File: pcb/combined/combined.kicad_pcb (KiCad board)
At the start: 2 copper layers, 65 x 38 mm, 34 parts, among them J1 CTRL, J2 MAINS_IN, J3 VALVE, J4 PUMP, Q1 SS8050, Q2 BT136S, Q3 SS8050, Q4 BT136S, U1 MOC3043M, U2 MOC3023M, U3 EL817C

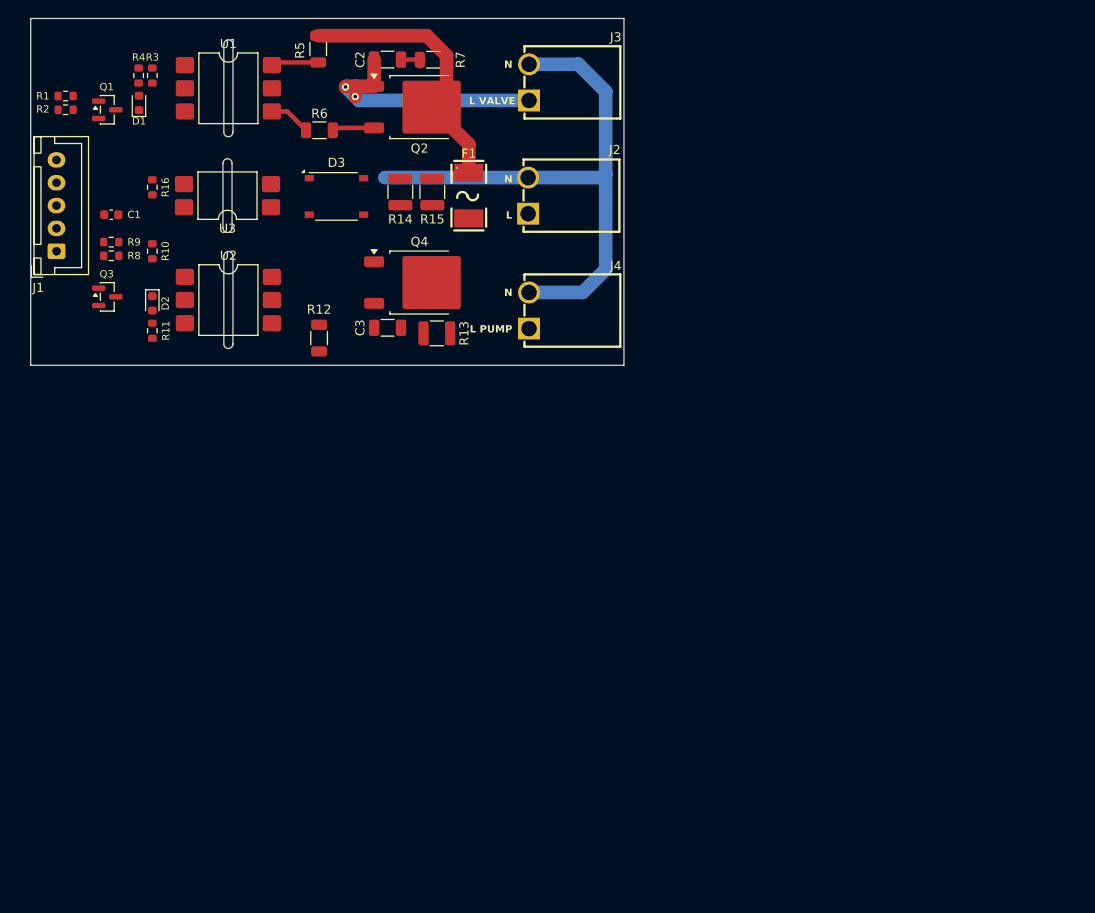
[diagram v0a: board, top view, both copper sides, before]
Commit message: Combine the AC control and sensors circuits on the combined board
The renamed accontrol project now carries the sensors controller on two
new sheets: XIAO, CAN, I2C pull-ups with TMP102 and ADS1115, FLOW, boiler
output, status LED and the 5 V, CAN, BOILER, PRESSURE and FLOW headers.
The 5-pin control header, the Grove I2C headers and the VALVE header are
dropped: DIM, ZC and SSR run as tracks to XIAO D0, D2 and D10. Sensors
parts that clashed with AC references are renumbered, the BOM and design
notes follow, and +5V/+3V3 get the 0.3 mm POWER net class from sensors.

Co-Authored-By: Claude Opus 5.5 <noreply@anthropic.com>
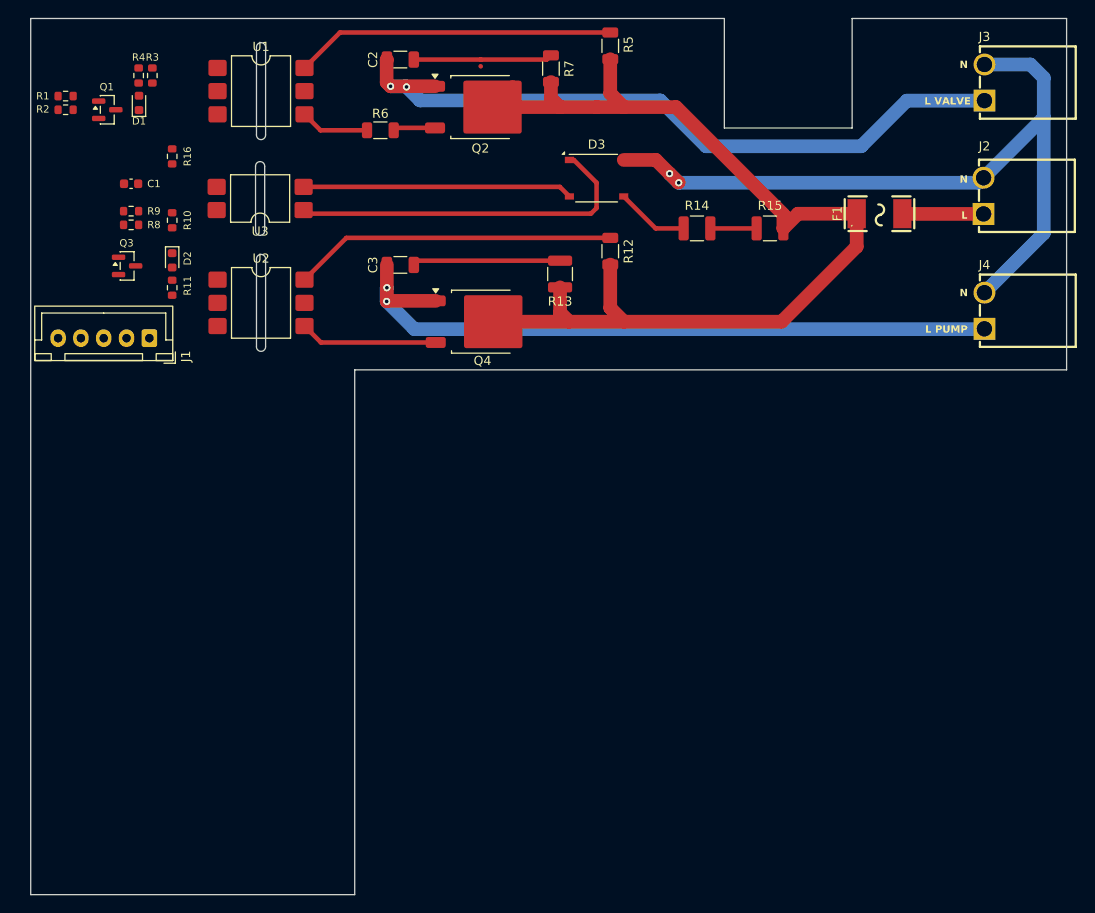
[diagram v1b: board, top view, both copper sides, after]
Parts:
- F1: footprint Accontrol_Local:F2410 -> Combined_Local:F2410
- J2, J3, J4: footprint Accontrol_Local:CONN-TH_P3.96_HT396R-3.96-2P -> Combined_Local:CONN-TH_P3.96_HT396R-3.96-2P
- U1, U2: footprint Accontrol_Local:SMDIP-6_W9.53mm_Slot -> Combined_Local:SMDIP-6_W9.53mm_Slot
- U3: footprint Accontrol_Local:SMDIP-4_W9.53mm_Slot -> Combined_Local:SMDIP-4_W9.53mm_Slot
- moved J2 49.9 mm to (184.9, 66.4)
- moved J3 49.9 mm to (185.0, 54.0)
- moved J4 49.9 mm to (185.0, 79.0)
- moved F1 45.0 mm to (173.5, 68.4), turned to 0 degrees
- moved R15 37.2 mm to (161.5, 70.0), turned to 0 degrees
- moved R12 33.3 mm to (144.0, 72.5)
- moved R14 32.7 mm to (153.5, 70.0), turned to 0 degrees
- moved R5 32.0 mm to (144.0, 50.0), turned to -90 degrees
- moved D3 28.6 mm to (142.5, 64.5)
- moved R13 15.0 mm to (138.5, 75.0), turned to 90 degrees
- moved J1 13.9 mm to (93.5, 82.0), turned to 180 degrees
- moved R7 12.9 mm to (137.5, 52.5), turned to 90 degrees
- moved Q4 8.00 mm to (129.9, 80.2)
- moved C3 7.03 mm to (121.0, 74.0)
- moved Q2 6.67 mm to (129.8, 56.7)
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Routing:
- net /L: track 30.2 -> 117.0 mm
- net /L_PUMP: track 0.00 -> 77.6 mm, vias 0 -> 2
- net /L_VALVE: track 27.9 -> 77.9 mm
- net Net-(D3-+): track 0.00 -> 40.0 mm
- net Net-(R12-Pad1): track 0.00 -> 35.4 mm
- net Net-(R5-Pad1): track 5.38 -> 35.3 mm
- net Net-(D3--): track 0.00 -> 29.6 mm
- net /N: track 63.0 -> 84.8 mm, vias 0 -> 2
- net Net-(C3-Pad1): track 0.00 -> 16.2 mm
- net Net-(Q4-G): track 0.00 -> 15.1 mm
- net Net-(C2-Pad1): track 2.10 -> 15.3 mm
- net /L_IN: track 0.00 -> 8.91 mm
- net Net-(D3-Pad3): track 0.00 -> 8.01 mm
- net Net-(R14-Pad2): track 0.00 -> 5.07 mm
- net Net-(R6-Pad1): track 4.60 -> 7.57 mm
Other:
- board size 65 x 38 mm -> 113.5 x 96 mm

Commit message: Bring the sensors footprints onto the combined board and align the XIAO sockets
Update the combined PCB from the schematic, which adds the sensors
footprints and replaces the old 5-pin control header. A board-only XIAO
outline footprint, without pads or drills, marks the module and its 14 pin
centres; J11 (turned 180 degrees, DIM at the bottom) and J12 sit exactly
on those centres.

Co-Authored-By: Claude Opus 5.5 <noreply@anthropic.com>
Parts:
- added C10: 100nF, Capacitor_SMD:C_0603_1608Metric, F.Cu at (87.0, 63.0)
- added C12: 10nF, Capacitor_SMD:C_0603_1608Metric, F.Cu at (84.3, 80.0)
- added C13: 100nF, Capacitor_SMD:C_0603_1608Metric, F.Cu at (105.2, 111.5)
- added C14: 10uF, Capacitor_SMD:C_0603_1608Metric, F.Cu at (114.0, 111.5)
- added C15: 100nF, Capacitor_SMD:C_0603_1608Metric, F.Cu at (93.5, 123.5)
- added C8: 100nF, Capacitor_SMD:C_0603_1608Metric, F.Cu at (83.5, 114.5)
- added C9: 100nF, Capacitor_SMD:C_0603_1608Metric, F.Cu at (88.0, 114.5)
- added D4: GREEN / STATUS, LED_SMD:LED_0805_2012Metric, F.Cu at (104.5, 134.5)
- added H1: M2.5, MountingHole:MountingHole_2.7mm_M2.5, F.Cu at (93.5, 140.0)
- added J10: PRESSURE, Connector_JST:JST_XH_B3B-XH-A_1x03_P2.50mm_Vertical, F.Cu at (95.5, 128.4)
- added J11: XIAO D0-D6, Combined_Local:XIAO_Socket_1x07_P2.54mm_Vertical, F.Cu at (99.2, 103.2)
- added J12: XIAO D7-5V, Combined_Local:XIAO_Socket_1x07_P2.54mm_Vertical, F.Cu at (84.0, 88.0)
- added J5: CAN BUS, Connector_JST:JST_XH_B2B-XH-A_1x02_P2.50mm_Vertical, F.Cu at (83.5, 139.0)
- added J6: FLOW HALL, Connector_JST:JST_XH_B3B-XH-A_1x03_P2.50mm_Vertical, F.Cu at (83.5, 128.4)
- added J8: BOILER SSR, Connector_JST:JST_XH_B2B-XH-A_1x02_P2.50mm_Vertical, F.Cu at (98.0, 120.0)
- added Q5: AO3401A, Package_TO_SOT_SMD:SOT-23, F.Cu at (105.6, 106.0)
- added Q6: 2N7002, Package_TO_SOT_SMD:SOT-23, F.Cu at (103.1, 101.0)
- added R17: 10k, Resistor_SMD:R_0603_1608Metric, F.Cu at (93.0, 114.5)
- added R18: 120 / 0.25W, Resistor_SMD:R_1206_3216Metric, F.Cu at (82.0, 120.5)
- added R19: 100k, Resistor_SMD:R_0603_1608Metric, F.Cu at (99.5, 110.5)
- added R20: 4.7k, Resistor_SMD:R_0603_1608Metric, F.Cu at (96.3, 83.0)
- added R21: 10k, Resistor_SMD:R_0603_1608Metric, F.Cu at (106.7, 101.5)
- added R22: 1k, Resistor_SMD:R_0603_1608Metric, F.Cu at (98.5, 114.0)
- added R23: 4.7k, Resistor_SMD:R_0603_1608Metric, F.Cu at (93.3, 83.0)
- added R24: 1k, Resistor_SMD:R_0603_1608Metric, F.Cu at (84.2, 84.0)
- added R25: 1k, Resistor_SMD:R_0603_1608Metric, F.Cu at (99.0, 135.0)
- added R26: 1k, Resistor_SMD:R_0603_1608Metric, F.Cu at (111.0, 111.5)
- added U4: TJA1051T/3, Package_SO:SOIC-8_3.9x4.9mm_P1.27mm, F.Cu at (87.0, 120.6)
- added U5: TMP102AIDRLR, Package_TO_SOT_SMD:SOT-563, F.Cu at (83.7, 65.5)
- added U6: ADS1115IDGSR, Package_SO:TSSOP-10_3x3mm_P0.5mm, F.Cu at (107.0, 95.0)
- added XIAO: XIAO-ESP32-S3-Outline, Combined_Local:XIAO-ESP32-S3-Outline, F.Cu at (91.6, 95.6)
- J1: value CTRL -> 5V POWER; footprint Connector_JST:JST_XH_B5B-XH-A_1x05_P2.50mm_Vertical -> Connector_JST:JST_XH_B2B-XH-A_1x02_P2.50mm_Vertical
- moved J1 57.4 mm to (100.5, 139.0), turned to 0 degrees
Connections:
- J1 pad 2: +3V3 -> +5V
- R1 pad 1: /SSR -> SSR
- R16 pad 2: /ZC -> ZC
- R2 pad 1: /SSR -> SSR
- R8 pad 1: /DIM -> DIM
- R9 pad 1: /DIM -> DIM
- U3 pad 4: /ZC -> ZC
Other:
- outline, holes or cut-outs redrawn

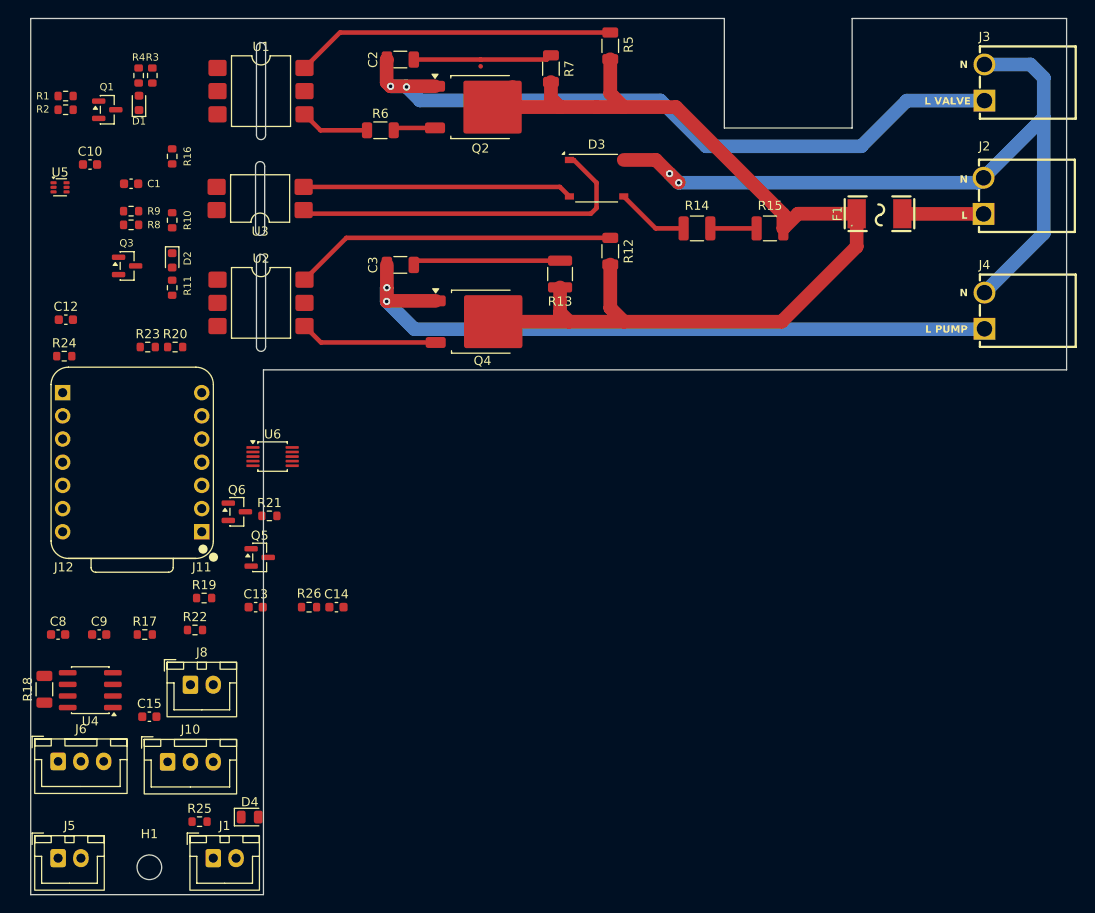
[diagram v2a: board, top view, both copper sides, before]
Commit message: Route the combined board to a clean DRC and export it for JLCPCB
Rules follow IEC 60335-1 for functional insulation: 2.2 mm between mains
nets, 1.5 mm or 1.1 mm between mains nets a few volts apart, and the
track-into-pad exception tied to the part a track enters. The HT3.96
connectors get oval pads, the datasheet's 1.6 mm holes and a milled slot
between L and N. C2/C3 move to 1812, R12 splits into R12 + R27, and every
part has its JLCPCB number. The exporter accepts polygon outlines, and the
placement corrections come from the supplier footprints. H2 and H3 are
added to the schematic.

Co-Authored-By: Claude Opus 5.5 <noreply@anthropic.com>
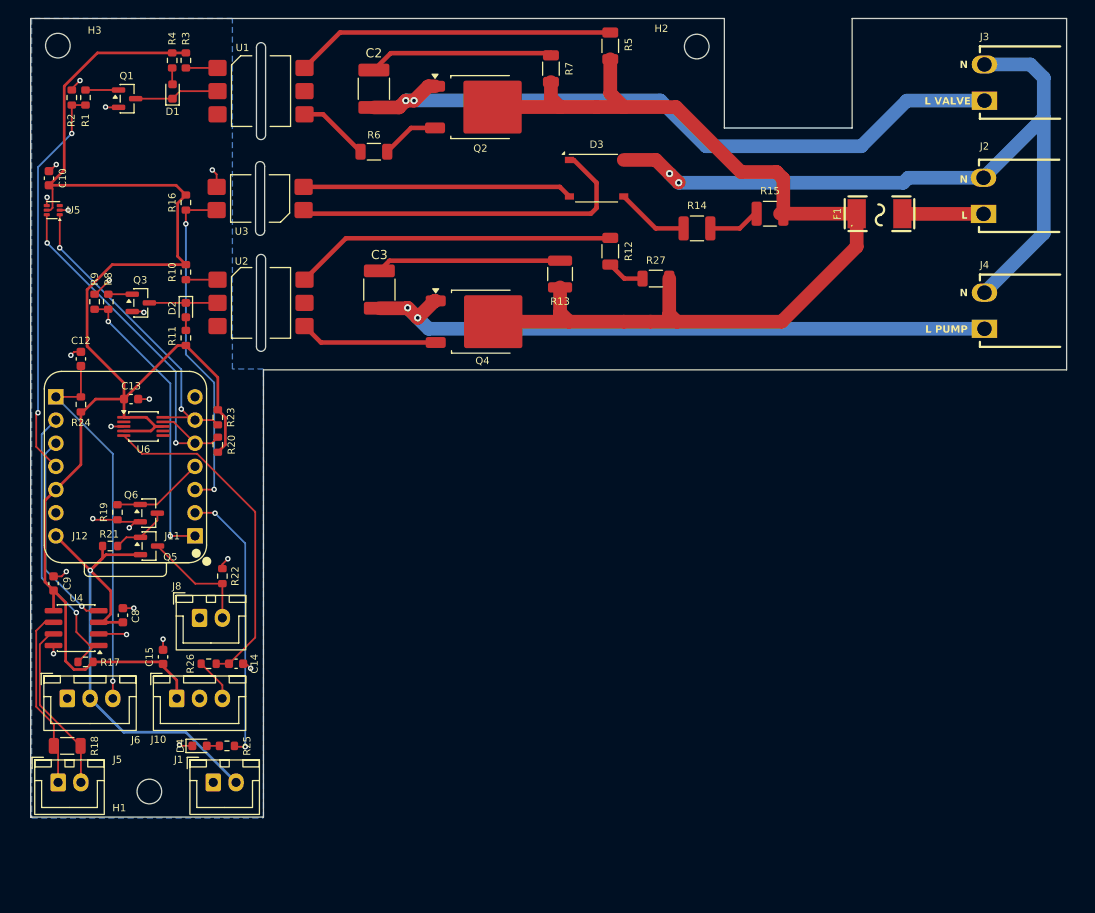
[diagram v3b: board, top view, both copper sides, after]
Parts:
- removed C1: 1uF, Capacitor_SMD:C_0603_1608Metric
- added H2: M2.5, MountingHole:MountingHole_2.7mm_M2.5, F.Cu at (153.5, 50.1)
- added H3: M2.5, MountingHole:MountingHole_2.7mm_M2.5, F.Cu at (83.5, 50.0)
- added R27: 510, Resistor_SMD:R_1206_3216Metric, F.Cu at (149.0, 75.5)
- C2, C3: footprint Capacitor_SMD:C_1206_3216Metric -> Capacitor_SMD:C_1812_4532Metric
- D4: value GREEN / STATUS -> STATUS; footprint LED_SMD:LED_0805_2012Metric -> LED_SMD:LED_0603_1608Metric
- R12: value 1k -> 510
- moved C13 26.6 mm to (91.5, 88.7)
- moved R21 17.8 mm to (89.2, 104.8)
- moved U6 14.5 mm to (92.8, 91.7)
- moved R19 13.4 mm to (90.0, 101.1), turned to -90 degrees
- moved C14 12.6 mm to (103.0, 117.7)
- moved R26 12.6 mm to (100.0, 117.7)
- moved Q5 12.2 mm to (93.5, 104.8)
- moved R20 11.7 mm to (101.0, 93.7), turned to 90 degrees
- moved R23 10.9 mm to (101.0, 90.7), turned to -90 degrees
- moved R9 10.7 mm to (87.5, 78.0), turned to 90 degrees
- moved Q6 9.65 mm to (93.4, 101.2)
- moved D4 9.54 mm to (99.0, 126.7)
- moved R25 8.83 mm to (102.0, 126.7), turned to 180 degrees
- moved R8 8.79 mm to (89.0, 78.0), turned to 90 degrees
- moved H1 8.30 mm to (93.5, 131.7)
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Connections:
- R12 pad 2: /L -> Net-(R12-Pad2)
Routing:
- net +3V3: track 0.00 -> 166.1 mm
- net +5V: track 0.00 -> 60.2 mm, vias 0 -> 1
- net SSR: track 0.00 -> 43.6 mm, vias 0 -> 2
- net FLOW_PULSE: track 0.00 -> 41.7 mm, vias 0 -> 1
- net I2C_SDA: track 0.00 -> 40.2 mm, vias 0 -> 2
- net ZC: track 0.00 -> 37.4 mm, vias 0 -> 2
- net PRESSURE_ADC: track 0.00 -> 37.1 mm
- net I2C_SCL: track 0.00 -> 35.2 mm, vias 0 -> 2
- net GND: track 0.00 -> 34.2 mm, vias 0 -> 21
- net DIM: track 0.00 -> 31.9 mm, vias 0 -> 2
- net CAN_TX: track 0.00 -> 31.5 mm, vias 0 -> 1
- net /Controller/STATUS_LED: track 0.00 -> 30.4 mm, vias 0 -> 2
- net CAN_RX: track 0.00 -> 22.0 mm, vias 0 -> 1
- net /Interfaces/CAN_L: track 0.00 -> 19.9 mm
- net /Interfaces/CAN_H: track 0.00 -> 19.0 mm
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- added copper zone on B.Cu, net GND
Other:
- board size 113.5 x 96 mm -> 113.5 x 87.5 mm
